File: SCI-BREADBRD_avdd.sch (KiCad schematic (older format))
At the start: 25 parts

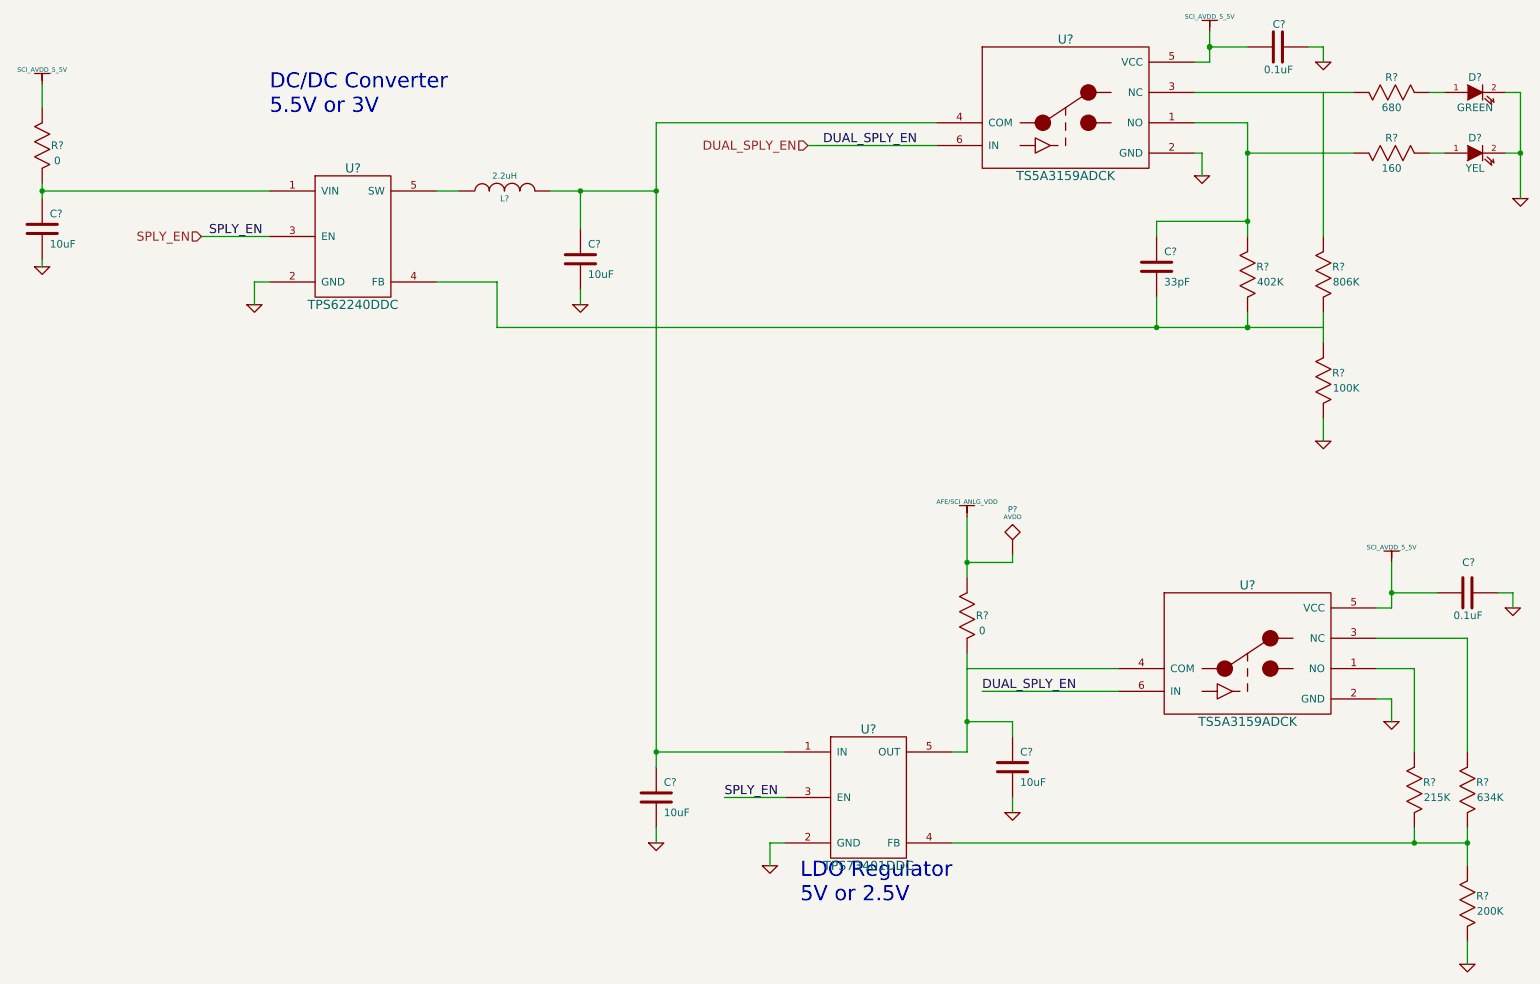
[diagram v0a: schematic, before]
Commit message: Fixed the footprint properties of various parts throughout the schematic to make sure they are all point to valid footprints.
Added SCI-BREADBRD.cmp to specify which footprints should be used for
each part.

Added netlists to the .gitignore as those can be generated easily in
eeschema.
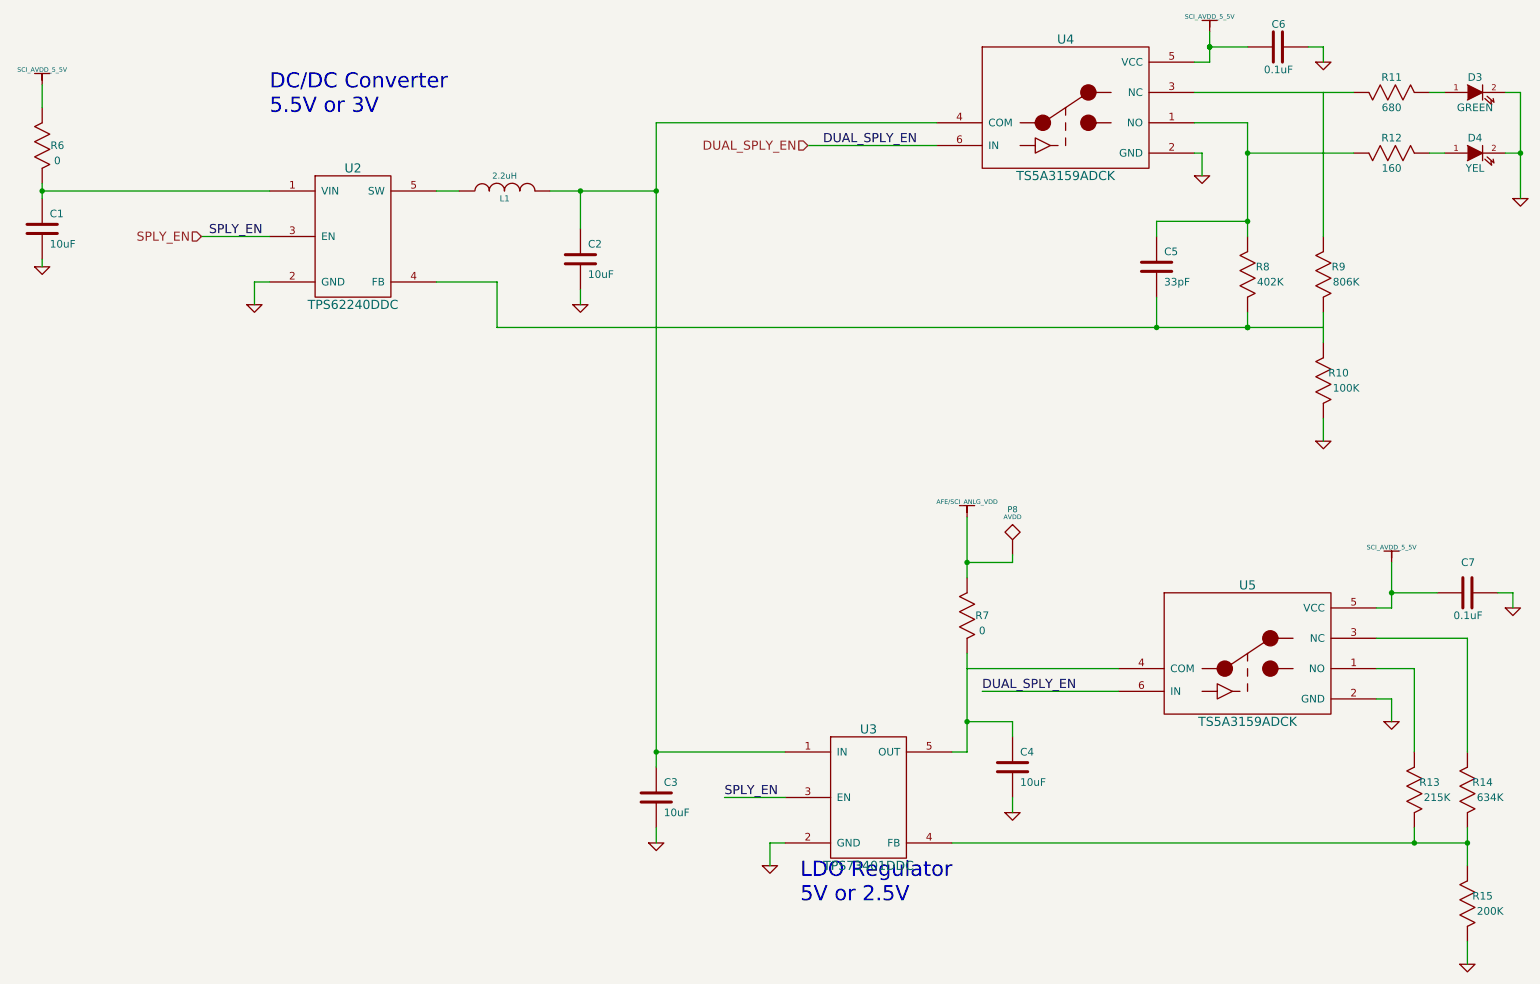
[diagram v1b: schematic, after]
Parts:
- C1, C2, C3, C4: renamed from C?; footprint SM0603 -> 0603
- C5, C6, C7: renamed from C?; footprint SM0402 -> 0402
- D3, D4: renamed from D?; footprint SM0402 -> 0402
- L1: renamed from L?; footprint SM1008 -> 1008
- R10, R11, R12, R13, R14, R15, R8, R9: renamed from R?; footprint SM0402 -> 0402
- R6, R7: renamed from R?; footprint SM0603 -> 0603
- gave numbers to parts that had none: 5
